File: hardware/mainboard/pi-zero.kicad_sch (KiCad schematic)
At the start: 18 parts, among them J13 USB_A_Stacked, J2 USB_A, T1 5V, T1 D+, T1 D-, T1 Gnd, T1 RXD, T1 Shield, T1 TXD

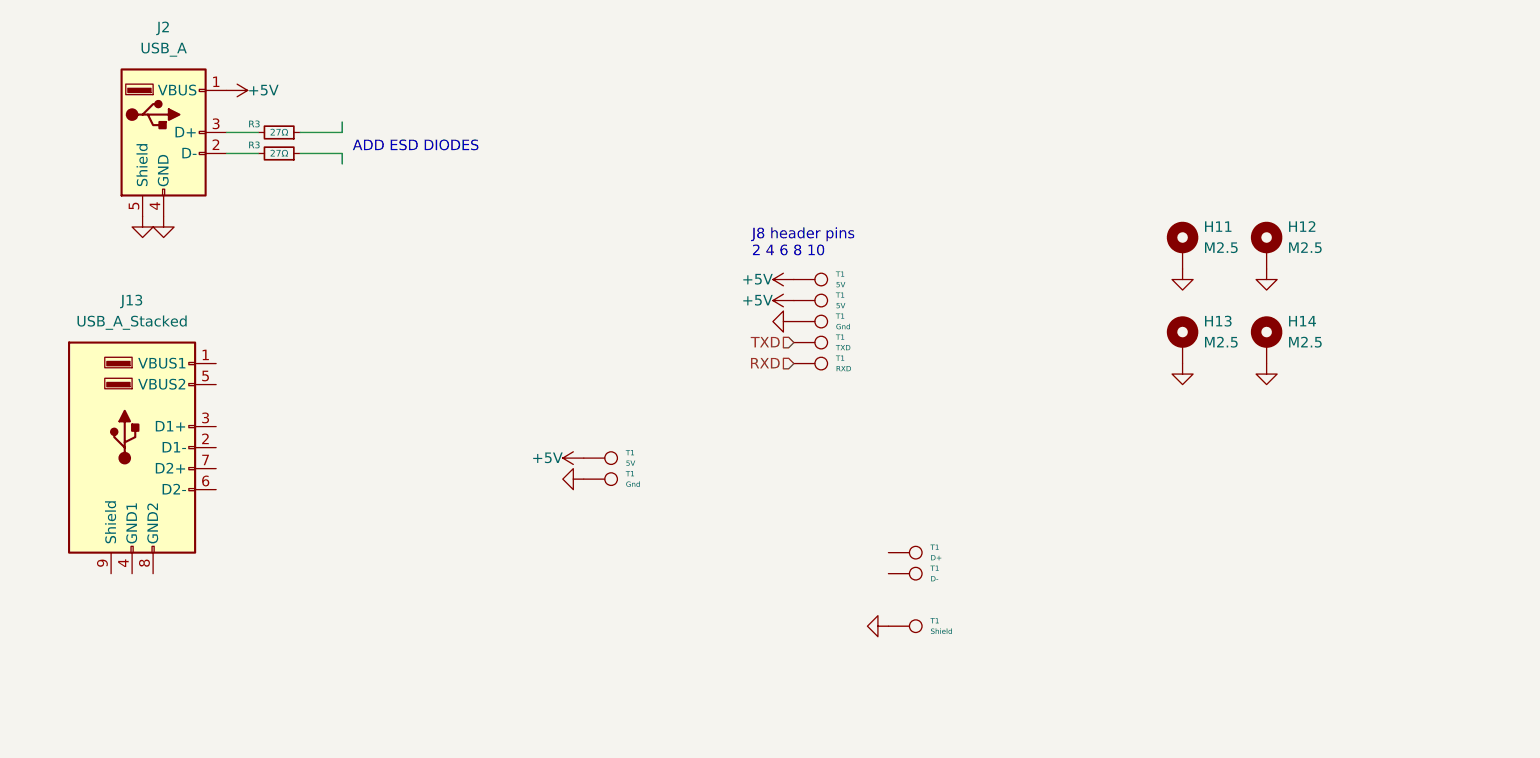
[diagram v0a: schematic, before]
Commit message: saving mainboard, gonna tear out the entire thing and redo in 4-layer
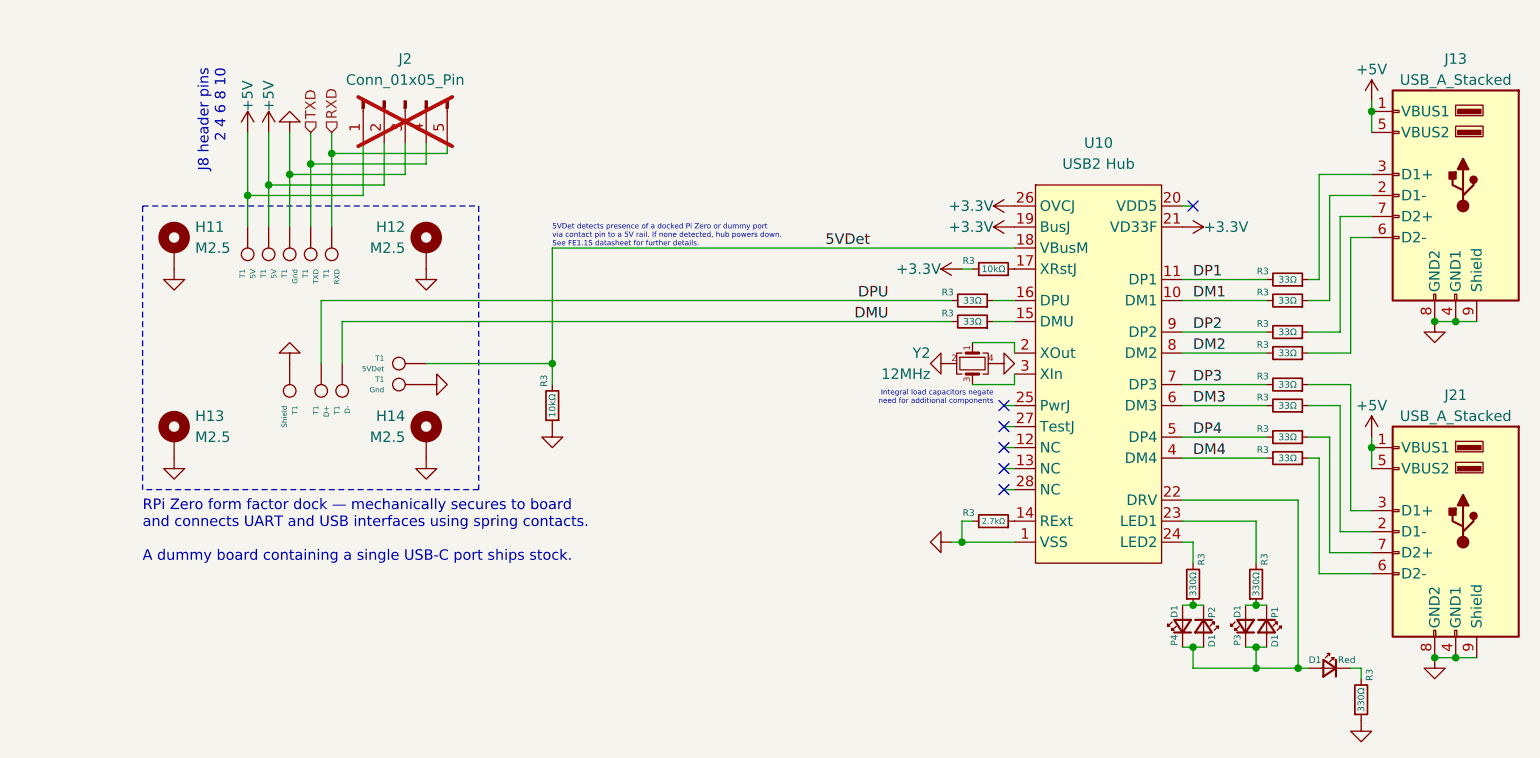
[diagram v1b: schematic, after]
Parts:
- removed J2: USB_A, symbol Connector:USB_A
- removed R3 (x2): 27Ω, symbol Device:R_Small
- removed T1: 5V, corevus:LGA_Spring, symbol Connector:TestPoint
- removed T1: Gnd, corevus:LGA_Spring, symbol Connector:TestPoint
- added D1: P4, AlphaLib:0603LED, symbol Device:LED_Small
- added D1: Red, AlphaLib:0603LED, symbol Device:LED_Small
- added D1: P2, AlphaLib:0603LED, symbol Device:LED_Small
- added D1: P3, AlphaLib:0603LED, symbol Device:LED_Small
- added D1: P1, AlphaLib:0603LED, symbol Device:LED_Small
- added J2: Conn_01x05_Pin, Connector_PinHeader_2.54mm:PinHeader_1x05_P2.54mm_Vertical, symbol Connector:Conn_01x05_Pin
- added J21: USB_A_Stacked, Connector_USB:USB_A_CUI_UJ2-ADH-TH_Horizontal_Stacked, symbol Connector:USB_A_Stacked
- added R3 (x10): 33Ω, AlphaLib:0402R, symbol Device:R_Small
- added R3 (x3): 330Ω, AlphaLib:0603R, symbol Device:R_Small
- added R3 (x2): 10kΩ, AlphaLib:0603R, symbol Device:R_Small
- added R3: 2.7kΩ, AlphaLib:0603R, symbol Device:R_Small
- added T1: 5VDet, corevus:LGA_Spring, symbol Connector:TestPoint
- added T1: Gnd, corevus:LGA_Spring, symbol Connector:TestPoint
- added U10: USB2 Hub, Package_SO:SSOP-28_3.9x9.9mm_P0.635mm, symbol corevus:FE1.1s-BSOP28B
- added Y2: 12MHz, Crystal:Crystal_SMD_3225-4Pin_3.2x2.5mm, symbol Device:Crystal_GND24_Small
- J13: footprint (none) -> Connector_USB:USB_A_CUI_UJ2-ADH-TH_Horizontal_Stacked
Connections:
- net +5V: now also J13.1 (VBUS1), J13.5 (VBUS2), J2.1 (Pin_1), J2.2 (Pin_2), J21.1 (VBUS1), J21.5 (VBUS2)
- net GND: now also J13.4 (GND1), J13.8 (GND2), J13.9 (Shield), J2.3 (Pin_3), J21.4 (GND1), J21.8 (GND2), J21.9 (Shield), R3.1, R3.1, R3.2, T1.1, U10.1 (VSS), Y2.2, Y2.4
- net RXD: now also J2.5 (Pin_5)
- net TXD: now also J2.4 (Pin_4)
- net DMU: now reaches T1.1
- net DMU: now also R3.2
- net at J13.2 (D1-): now also R3.1
- net at J13.3 (D1+): now also R3.1
- net at J13.6 (D2-): now also R3.1
- net at J13.7 (D2+): now also R3.1
- net DPU: now reaches T1.1
- net DPU: now also R3.2
- new net: U10.2 (XOut), Y2.1
- new net: U10.3 (XIn), Y2.3
- new net: J21.3 (D1+), R3.1
- new net: J21.2 (D1-), R3.1
- new net: J21.6 (D2-), R3.1
- new net: J21.7 (D2+), R3.1
- new net: R3.1, U10.14 (RExt)
- new net: R3.1, U10.15 (DMU)
- new net: R3.1, U10.16 (DPU)
- new net: R3.1, U10.17 (XRstJ)
- new net: D1.1 (K), D1.1 (K), D1.2 (A), D1.2 (A), D1.2 (A), U10.22 (DRV)
- new net: R3.2, U10.23 (LED1)
- new net: R3.2, U10.24 (LED2)
- new net: D1.1 (K), D1.2 (A), R3.1 (x2)
- new net: D1.1 (K), R3.2
- new net +3.3V: R3.2, U10.19 (BusJ), U10.21 (VD33F), U10.26 (OVCJ)
- new net 5VDet: R3.2, T1.1, U10.18 (VBusM)
- new net DM1: R3.2, U10.10 (DM1)
- new net DM2: R3.2, U10.8 (DM2)
- new net DM3: R3.2, U10.6 (DM3)
- new net DM4: R3.2, U10.4 (DM4)
- new net DP1: R3.2, U10.11 (DP1)
- new net DP2: R3.2, U10.9 (DP2)
- new net DP3: R3.2, U10.7 (DP3)
- new net DP4: R3.2, U10.5 (DP4)
- no-connect marks 0 -> 6
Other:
- note added: "5VDet detects presence of a docked Pi Zero or dummy port via contact pin to a 5V rail. If none detected, hub powers down. See FE1.1S datasheet for further details."
- note added: "Integral load capacitors negate need for additional components"
- note added: "RPi Zero form factor dock — mechanically secures to board and connects UART and USB interfaces using spring contacts. A dummy board containing a single USB-C port ships stock."
- note removed: "ADD ESD DIODES"
- moved on the sheet: H11, H12, H13, H14, J13, T1

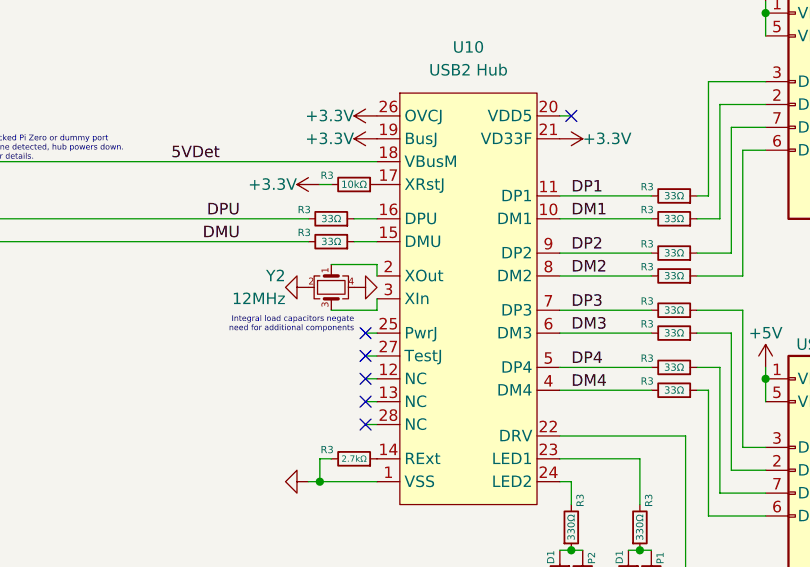
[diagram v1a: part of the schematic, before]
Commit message: further board edits, mostly done with power planes, heaters, fans, motor channels, starting work on microcontroller signals
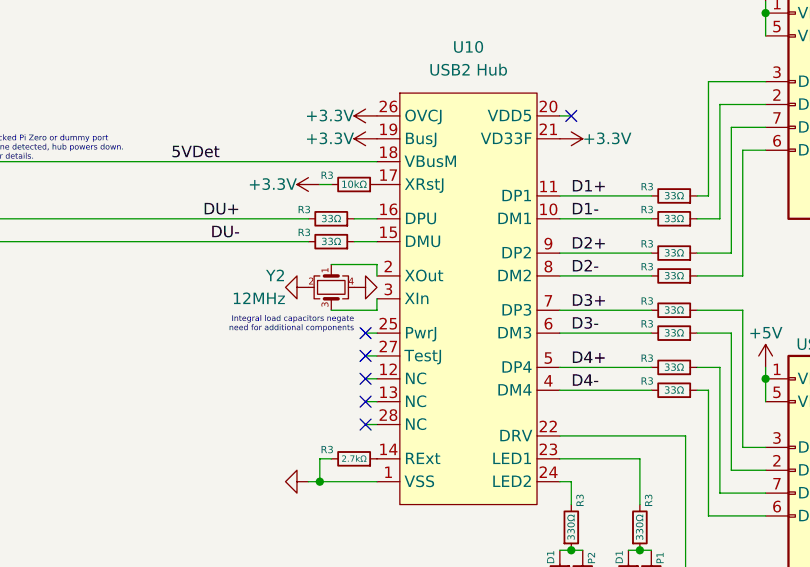
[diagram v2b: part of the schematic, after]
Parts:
- R3: footprint AlphaLib:0603R -> AlphaLib:0402R
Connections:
- net DM1 renamed D1-
- net DM2 renamed D2-
- net DM3 renamed D3-
- net DM4 renamed D4-
- net DMU renamed DU-
- net DP1 renamed D1+
- net DP2 renamed D2+
- net DP3 renamed D3+
- net DP4 renamed D4+
- net DPU renamed DU+
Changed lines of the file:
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@@
     (effects (font (size 1.27 1.27)) (justify right bottom))
   )
-  (label "DP2" (at 156.21 52.07 0) (fields_autoplaced)
+  (label "D2+" (at 156.21 52.07 0) (fields_autoplaced)
     (effects (font (size 1.27 1.27)) (justify left bottom))
   )
-  (label "DM2" (at 156.21 54.61 0) (fields_autoplaced)
+  (label "D2-" (at 156.21 54.61 0) (fields_autoplaced)
     (effects (font (size 1.27 1.27)) (justify left bottom))
   )
-  (label "DP3" (at 156.21 58.42 0) (fields_autoplaced)
+  (label "D3+" (at 156.21 58.42 0) (fields_autoplaced)
     (effects (font (size 1.27 1.27)) (justify left bottom))
   )
-  (label "DM1" (at 156.21 48.26 0) (fields_autoplaced)
+  (label "D1-" (at 156.21 48.26 0) (fields_autoplaced)
     (effects (font (size 1.27 1.27)) (justify left bottom))
   )
-  (label "DM4" (at 156.21 67.31 0) (fields_autoplaced)
+  (label "D4-" (at 156.21 67.31 0) (fields_autoplaced)
     (effects (font (size 1.27 1.27)) (justify left bottom))
   )
-  (label "DMU" (at 119.38 50.8 180) (fields_autoplaced)
+  (label "DU-" (at 119.38 50.8 180) (fields_autoplaced)
     (effects (font (size 1.27 1.27)) (justify right bottom))
   )
-  (label "DPU" (at 119.38 48.26 180) (fields_autoplaced)
+  (label "DU+" (at 119.38 48.26 180) (fields_autoplaced)
     (effects (font (size 1.27 1.27)) (justify right bottom))
   )
-  (label "DP1" (at 156.21 45.72 0) (fields_autoplaced)
+  (label "D1+" (at 156.21 45.72 0) (fields_autoplaced)
     (effects (font (size 1.27 1.27)) (justify left bottom))
   )
@@
     (effects (font (size 1.27 1.27)) (justify left bottom))
   )
-  (label "DP4" (at 156.21 64.77 0) (fields_autoplaced)
+  (label "D4+" (at 156.21 64.77 0) (fields_autoplaced)
     (effects (font (size 1.27 1.27)) (justify left bottom))
   )
-  (label "DM3" (at 156.21 60.96 0) (fields_autoplaced)
+  (label "D3-" (at 156.21 60.96 0) (fields_autoplaced)
     (effects (font (size 1.27 1.27)) (justify left bottom))
   )
@@
       (effects (font (size 0.8 0.8)))
     )
-    (property "Footprint" "AlphaLib:0603R" (at 156.21 82.55 0)
+    (property "Footprint" "AlphaLib:0402R" (at 156.21 82.55 0)
       (effects (font (size 1.27 1.27)) hide)
     )
@@
       (effects (font (size 0.8 0.8)))
     )
-    (property "Footprint" "AlphaLib:0603R" (at 176.53 96.52 0)
+    (property "Footprint" "AlphaLib:0402R" (at 176.53 96.52 0)
       (effects (font (size 1.27 1.27)) hide)
     )
@@
       (effects (font (size 0.8 0.8)))
     )
-    (property "Footprint" "AlphaLib:0603R" (at 163.83 82.55 0)
-      (effects (font (size 1.27 1.27)) hide)
-    )
+    (property "Footprint" "AlphaLib:0402R" (at 163.83 82.55 0)
+      (effects (font (size 1.27 1.27)) hide)
+    )

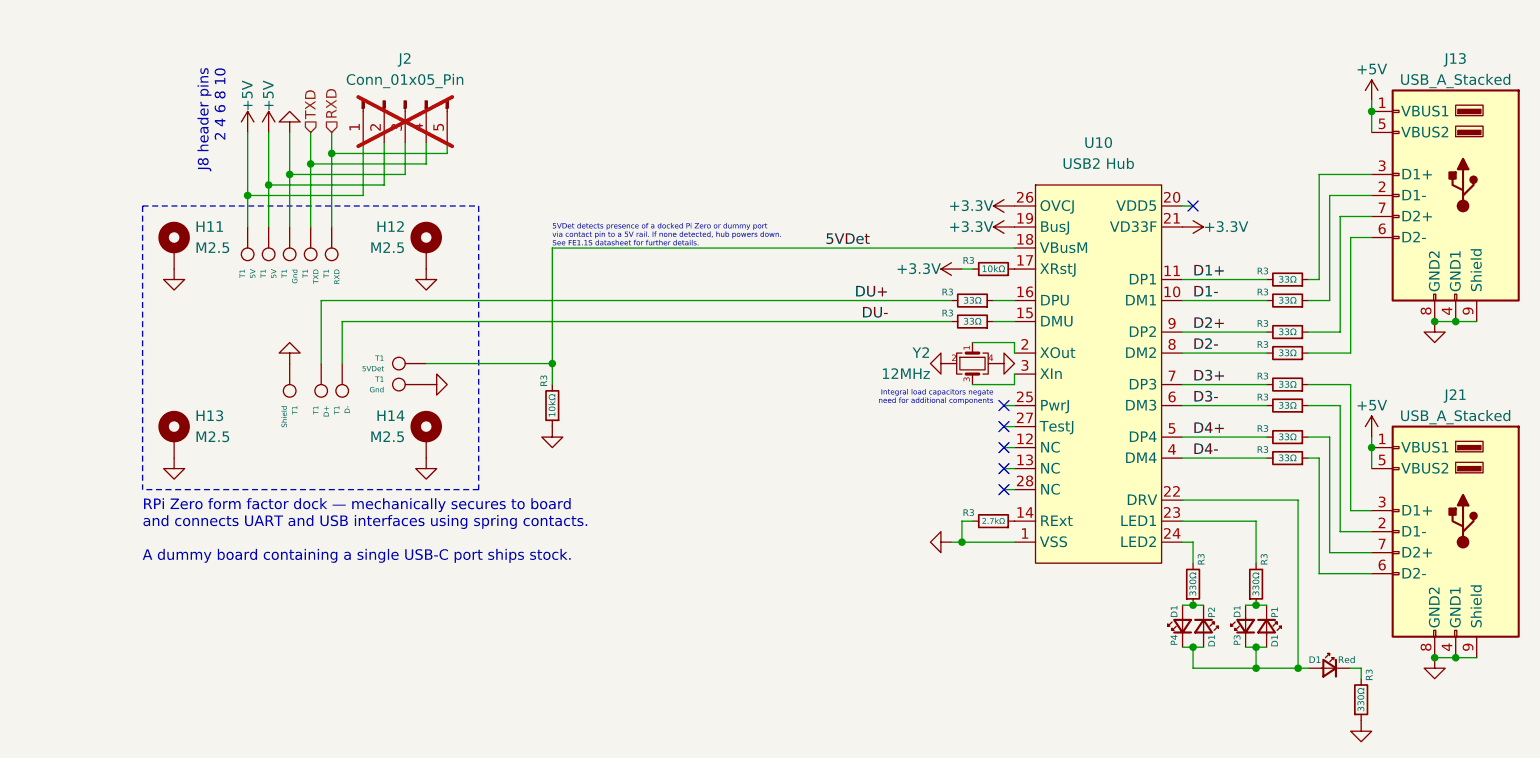
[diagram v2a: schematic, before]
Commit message: redid mainboard, added probe wiring, replacing ncp chip with LM5160 for now
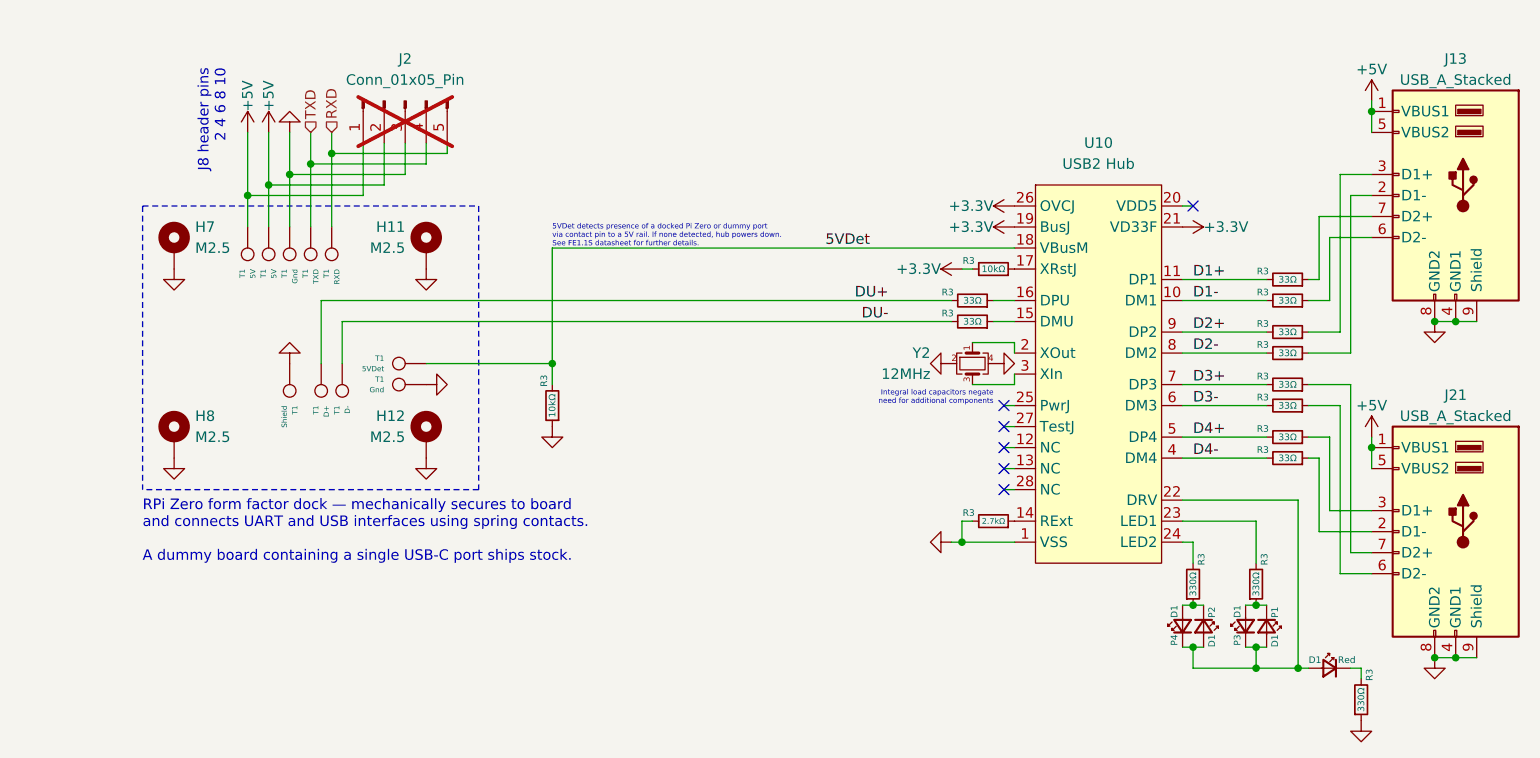
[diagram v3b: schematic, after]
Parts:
- J2: now left out of the parts list
- R3: footprint AlphaLib:0603R -> AlphaLib:0402R
- renumbered H12 to H11, H14 to H12, H11 to H7, H13 to H8
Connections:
- net at R3.1: now also J21.7 (D2+); no longer J21.3 (D1+)
- net at J13.2 (D1-): now also R3.1; no longer R3.1
- net at J13.3 (D1+): now also R3.1; no longer R3.1
- net at J13.6 (D2-): now also R3.1; no longer R3.1
- net at J13.7 (D2+): now also R3.1; no longer R3.1
- net at J21.2 (D1-): now also R3.1; no longer R3.1
- net at J21.6 (D2-): now also R3.1; no longer R3.1
- net at R3.1: now also J21.3 (D1+); no longer J21.7 (D2+)

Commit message: nearing first prototype woot! copyediting over entire board, fixed some mistakes
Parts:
- removed T1: Gnd, corevus:LGA_Spring, symbol Connector:TestPoint
- removed U10: USB2 Hub, Package_SO:SSOP-28_3.9x9.9mm_P0.635mm, symbol corevus:FE1.1s-BSOP28B
- added C10: 100nF, AlphaLib:0402C, symbol Device:C_Small
- added J22: FPC 8p 0.5mm, Connector_FFC-FPC:Hirose_FH12-8S-0.5SH_1x08-1MP_P0.50mm_Horizontal, symbol Connector_Generic:Conn_01x08
- added R3: 300Ω, AlphaLib:0402R, symbol Device:R_Small
- added T1: Gnd, corevus:LGA_Spring_3.5x1, symbol Connector:TestPoint
- added T1: MOSI, corevus:LGA_Spring_3.5x1, symbol Connector:TestPoint
- added T1: V_{CC}, corevus:LGA_Spring_3.5x1, symbol Connector:TestPoint
- added T1: MISO, corevus:LGA_Spring_3.5x1, symbol Connector:TestPoint
- added T1: CS, corevus:LGA_Spring_3.5x1, symbol Connector:TestPoint
- added T1: SClk, corevus:LGA_Spring_3.5x1, symbol Connector:TestPoint
- added U16: USB2 Hub, Package_SO:SSOP-28_3.9x9.9mm_P0.635mm, symbol corevus:FE1.1s-BSOP28B
- R3: value 2.7kΩ -> 2.4kΩ
- T1: footprint corevus:LGA_Spring -> corevus:LGA_Spring_3.5x1
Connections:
- net +3.3V: now also C10.2, U16.19 (BusJ), U16.21 (VD33F), U16.26 (OVCJ)
- net 5VDet: now also U16.18 (VBusM)
- net D1+: now also U16.11 (DP1)
- net D1-: now also U16.10 (DM1)
- net D2+: now also U16.9 (DP2)
- net D2-: now also U16.8 (DM2)
- net D3+: now also U16.7 (DP3)
- net D3-: now also U16.6 (DM3)
- net D4+: now also U16.5 (DP4)
- net D4-: now also U16.4 (DM4)
- net GND: now also C10.1, J22.1 (Pin_1), R3.2, T1.1, U16.1 (VSS); no longer R3.2
- net at Y2.1: now also U16.2 (XOut)
- net at Y2.3: now also U16.3 (XIn)
- net at R3.1: now also U16.14 (RExt)
- net at R3.1: now also U16.15 (DMU)
- net at R3.1: now also U16.16 (DPU)
- net at R3.1: now also U16.17 (XRstJ)
- net at D1.1 (K), D1.1 (K), D1.2 (A)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: now also U16.22 (DRV)
- net at R3.2: now also U16.23 (LED1)
- net at R3.2: now also U16.24 (LED2)
- new net: J22.7 (Pin_7), T1.1
- new net: J22.2 (Pin_2), T1.1
- new net: R3.1, R3.2
- new net: J22.6 (Pin_6), T1.1
- new net: J22.3 (Pin_3), T1.1
- new net: J22.8 (Pin_8), T1.1
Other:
- moved on the sheet: H11, H12, H7, H8, J2, R3, T1

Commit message: redoing board for version alpha 0.2
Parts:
- renumbered H8 to H10, H7 to H9, J2 to J24, J22 to J25, J13 to J26, J21 to J27, U16 to U13

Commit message: fan ports
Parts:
- J24: footprint Connector_PinHeader_2.54mm:PinHeader_1x05_P2.54mm_Vertical -> Connector_PinHeader_2.54mm:PinHeader_1x04_P2.54mm_Vertical; symbol Connector:Conn_01x05_Pin -> Connector:Conn_01x04_Pin; now in the parts list
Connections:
- net +5V: no longer J24.2 (Pin_2)
- net GND: now also J24.2 (Pin_2); no longer J24.3 (Pin_3)
- net RXD: now also J24.4 (Pin_4); no longer J24.5 (Pin_5)
- net TXD: now also J24.3 (Pin_3); no longer J24.4 (Pin_4)
- no-connect marks 6 -> 7
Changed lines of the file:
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@@
   (no_connect (at 133.35 71.12))
   (no_connect (at 133.35 66.04))
+  (no_connect (at 40.64 29.21))
   (wire (pts (xy 154.94 74.93) (xy 163.83 74.93))
     (stroke (width 0) (type default))
@@
     )
   )
-  (symbol (lib_id "Connector:Conn_01x05_Pin") (at 45.72 24.13 90) (mirror x) (unit 1)
-    (in_bom no) (on_board yes) (dnp yes)
+  (symbol (lib_id "Connector:Conn_01x04_Pin") (at 45.72 24.13 90) (mirror x) (unit 1)
+    (in_bom yes) (on_board yes) (dnp yes)
     (property "Reference" "J24" (at 45.72 19.05 90)
       (effects (font (size 1.27 1.27)))
@@
       (effects (font (size 1.27 1.27)))
     )
-    (property "Footprint" "Connector_PinHeader_2.54mm:PinHeader_1x05_P2.54mm_Vertical" (at 45.72 24.13 0)
+    (property "Footprint" "Connector_PinHeader_2.54mm:PinHeader_1x04_P2.54mm_Vertical" (at 45.72 24.13 0)
       (effects (font (size 1.27 1.27)) hide)
     )
@@
     (pin "3")
     (pin "4")
-    (pin "5")
-    (instances
-      (project "mainboard"
+    (instances
+      (project "mainboard"
